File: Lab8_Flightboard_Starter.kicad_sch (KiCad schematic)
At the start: 66 parts, among them J1 Motor1, J10 ESC3_GND, J11 ESC4_VBAT, J12 ESC4_GND, J2 Motor2, J3 Motor3, J4 Motor4, J5 ESC1_VBAT, J6 ESC1_GND, J7 ESC2_VBAT, J8 ESC2_GND, J9 ESC3_VBAT, Q1 DMP6023LE-13, U1 Teensy4.0, U10 MPU6050_HiLetgo_GY521, U2 TPS62933, U4 LP5912-3.3DRV, U5 LP5912-3.3DRV, U6 NRF24L01_Breakout, U8 MPU6050_Adafruit, U9 LSM6DSO32_Adafruit

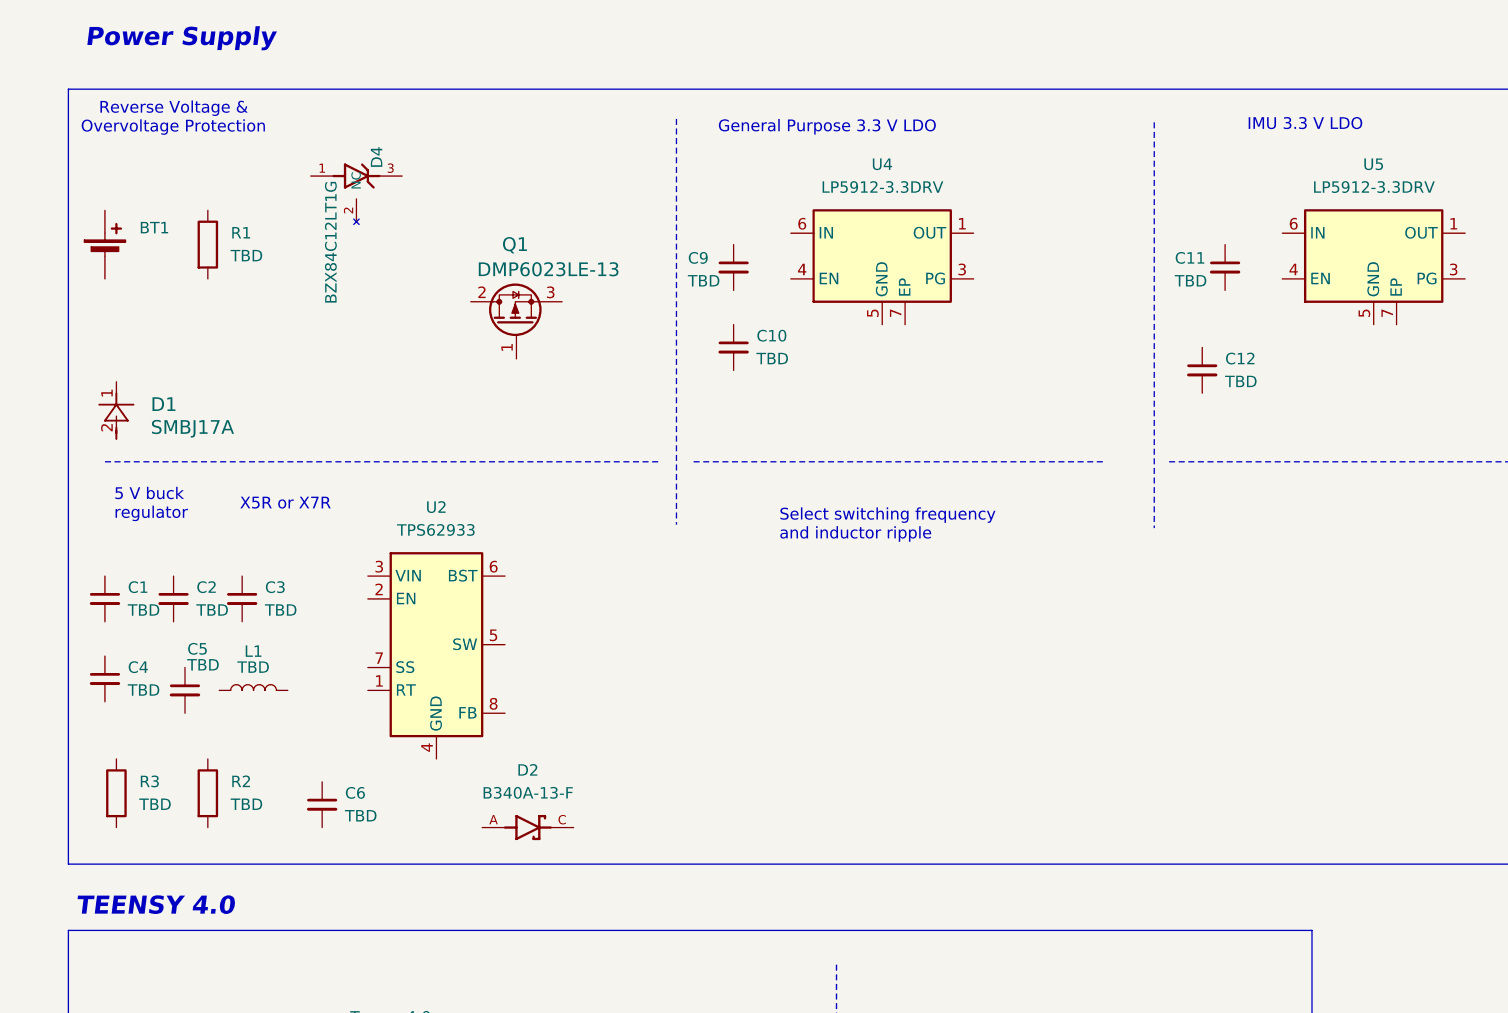
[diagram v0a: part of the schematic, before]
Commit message: Reverse voltage and 5V buck circuits
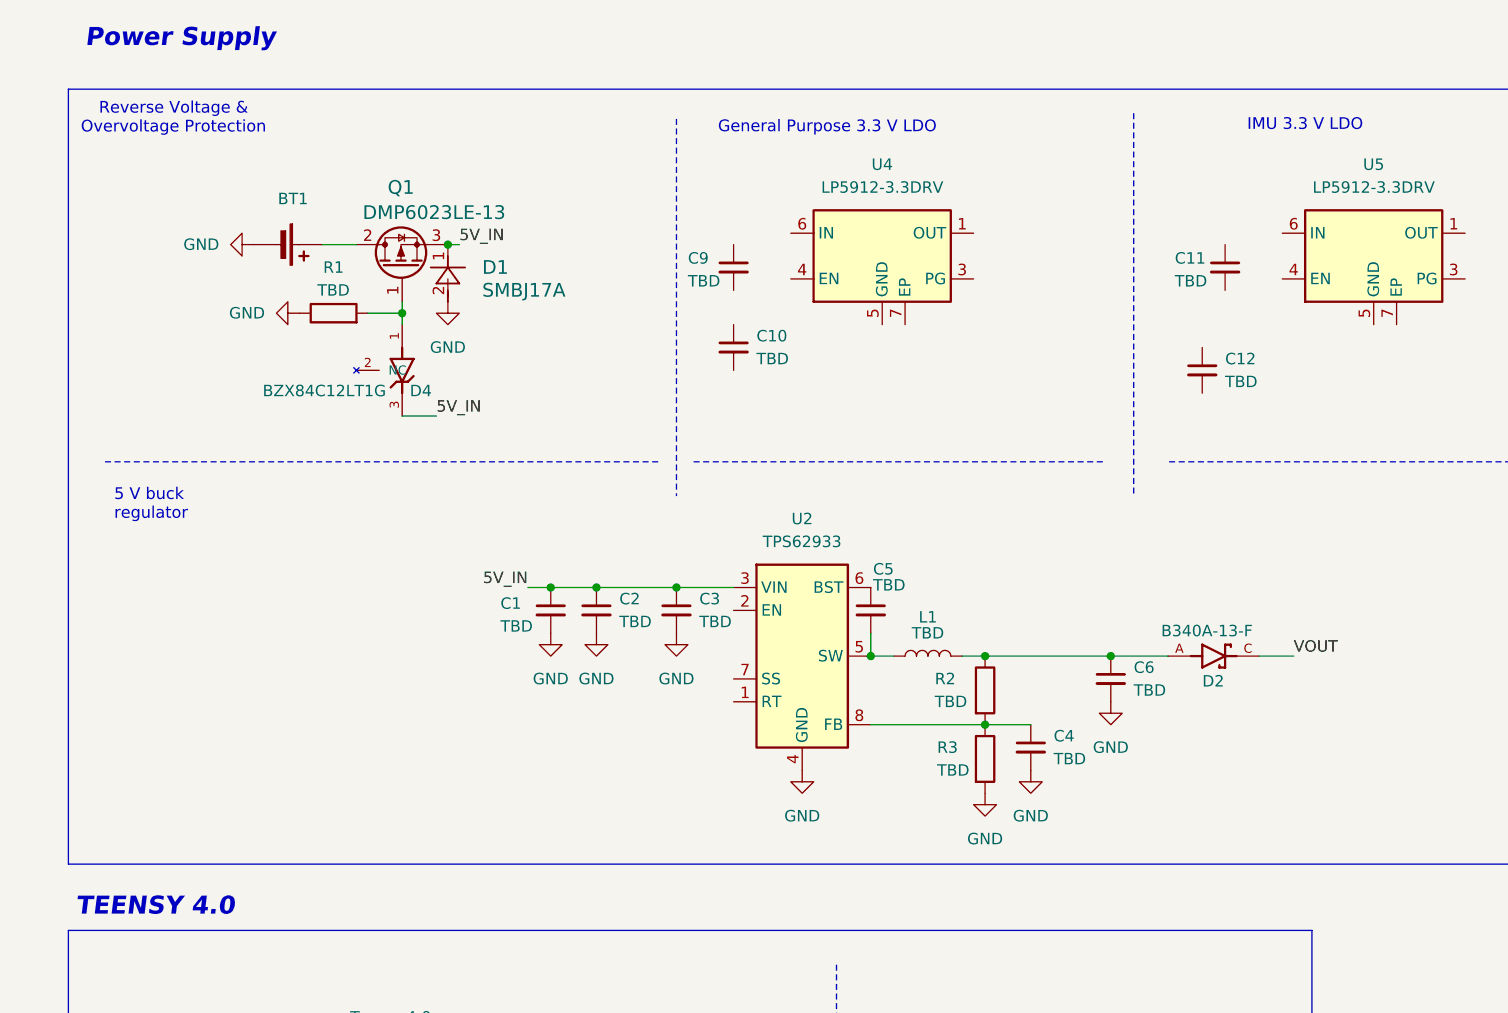
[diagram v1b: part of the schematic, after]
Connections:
- net at C4.1: now also R2.2, R3.1, U2.8 (FB)
- net GND: now reaches C4.2
- net GND: now also BT1.2 (-), C1.2, C2.2, C3.2, C6.2, D1.2, R1.1, R3.2, U2.4 (GND)
- net at C5.1: now also U2.6 (BST)
- net at C5.2: now also L1.1, U2.5 (SW)
- net at L1.2: now also C6.1, D2.A, R2.1
- net 5V_IN: now reaches C3.1
- net 5V_IN: now also C1.1, C2.1, D1.1, D4.3, Q1.3, U2.3 (VIN)
- net at R1.2: now also D4.1, Q1.1
- net at Q1.2: now also BT1.1 (+)
- net VOUT: now reaches D2.C
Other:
- note removed: "Select switching frequency and inductor ripple"
- note removed: "X5R or X7R"
- moved on the sheet: BT1, C1, C2, C3, C4, C5, C6, D1, D4, L1, Q1, R1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

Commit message: Circuit update V2
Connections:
- net GND: now also C4.1, U2.1 (RT), U5.5 (GND); no longer C4.2
- net at R2.2, R3.1, U2.8 (FB): no longer C4.1
- net at U2.7 (SS): now also C4.2
- net 5V_IN renamed LIPO_IN
- net VOUT renamed 5V_OUT
- no-connect marks 0 -> 1
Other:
- moved on the sheet: C1, C2, C3, C5, C6, D2, L1, R2, R3, U2

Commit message: Added values
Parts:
- C1, C2: value TBD -> 10u
- C3, C5: value TBD -> 0.1u
- C4: value TBD -> 33n
- C6: value TBD -> 20u
- L1: value TBD -> 6.8u
- R2: value TBD -> 55k
- R3: value TBD -> 10k
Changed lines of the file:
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@@
 		(in_pos_files yes)
 		(dnp no)
-		(fields_autoplaced yes)
 		(property "Reference" "C4"
-			(at 107.95 99.0538 0)
+			(at 104.394 96.774 0)
 			(show_name no)
 			(do_not_autoplace no)
@@
 					(size 1.27 1.27)
 				)
-				(justify left)
+				(justify right)
 			)
 		)
-		(property "Value" "TBD"
-			(at 107.95 96.5138 0)
+		(property "Value" "33n"
+			(at 104.394 99.06 0)
 			(show_name no)
 			(do_not_autoplace no)
@@
 					(size 1.27 1.27)
 				)
-				(justify left)
+				(justify right)
 			)
 		)
@@
 			)
 		)
-		(property "Value" "TBD"
+		(property "Value" "0.1u"
 			(at 129.794 81.026 0)
 			(show_name no)
@@
 			)
 		)
-		(property "Value" "TBD"
+		(property "Value" "10k"
 			(at 136.906 101.6 0)
 			(show_name no)
@@
 			)
 		)
-		(property "Value" "TBD"
+		(property "Value" "6.8u"
 			(at 135.89 86.36 90)
 			(show_name no)
@@
 			)
 		)
-		(property "Value" "TBD"
+		(property "Value" "55k"
 			(at 136.652 93.98 0)
 			(show_name no)
@@
 			)
 		)
-		(property "Value" "TBD"
+		(property "Value" "0.1u"
 			(at 106.68 85.0962 0)
 			(show_name no)
@@
 			)
 		)
-		(property "Value" "TBD"
+		(property "Value" "20u"
 			(at 149.86 92.7162 0)
 			(show_name no)
@@
 			)
 		)
-		(property "Value" "TBD"
+		(property "Value" "10u"
 			(at 84.582 85.598 0)
 			(show_name no)
@@
 			)
 		)
-		(property "Value" "TBD"
+		(property "Value" "10u"
 			(at 97.79 85.0962 0)
 			(show_name no)

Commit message: Motor signals
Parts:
- C6: value 20u -> 22u
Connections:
- net GND: now also J1.3 (Pin_3), J10.1 (Pin_1), J12.1 (Pin_1), J2.3 (Pin_3), J3.3 (Pin_3), J4.3 (Pin_3), J6.1 (Pin_1), J8.1 (Pin_1), R10.1, R12.1, R7.1, R8.1
- net MOTOR1: now reaches R6.1
- net MOTOR1: now also J1.1 (Pin_1), R7.2
- net M1_CMD: now reaches R6.2
- net MOTOR4: now reaches J4.1 (Pin_1)
- net MOTOR4: now also R12.2, R13.2
- net MOTOR3: now reaches R10.2
- net MOTOR3: now also J3.1 (Pin_1), R11.2
- net M4_CMD: now reaches R13.1
- net VBAT: now reaches J9.1 (Pin_1)
- net VBAT: now also BT1.1 (+), J11.1 (Pin_1), J5.1 (Pin_1), J7.1 (Pin_1), Q1.2
- net M2_CMD: now reaches R9.1
- net MOTOR2: now reaches R9.2
- net MOTOR2: now also J2.1 (Pin_1), R8.2
- net M3_CMD: now reaches R11.1
- no-connect marks 1 -> 5
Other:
- moved on the sheet: J1, J10, J11, J12, J2, J3, J4, J5, J6, J7, J8, J9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

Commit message: Edited circuits
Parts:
- C10, C11, C12, C9: value TBD -> 10u
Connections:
- net 5V_OUT: now also C9.1, U4.4 (EN), U4.6 (IN)
- net GND: now also C10.2, C11.2, C12.2, C13.2, C9.2, D3.1 (K), D6.1 (K), U4.5 (GND)
- net VBAT: now also R4.2
- net at R17.2: now also D3.2 (A)
- net 3.3V_GP: now reaches R15.1
- net 3.3V_GP: now also C10.1, U4.1 (OUT)
- net at R15.2: now also D6.2 (A)
- net at R5.2: now also C13.1, R4.1
- net 3.3V_IMU: now reaches C12.1
- net 3.3V_IMU: now also U5.1 (OUT)
- net at C11.1: now also U5.4 (EN), U5.6 (IN)
- net LIPO_IN renamed SYS_VIN
- no-connect marks 5 -> 9
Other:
- note removed: "Keep the ONE IMU module you bought; delete the other TWO symbols. U8: Adafruit MPU6050 | U10: HiLetgo GY-521 MPU6050 | U9: Adafruit LSM6DSO32 Use its matching footprint. All R/C/L values are TBD; complete wiring and pin allocation."
- moved on the sheet: C10, C11, C12, C13, C9, D3, D6, R15, R17, R4, U4

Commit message: More changes
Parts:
- removed U10: MPU6050_HiLetgo_GY521, IMU_Modules:MPU6050_HiLetgo_GY521, symbol IMU_Symbols:MPU6050_HiLetgo_GY521
- removed U8: MPU6050_Adafruit, IMU_Modules:MPU6050_Adafruit, symbol IMU_Symbols:MPU6050_Adafruit
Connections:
- net GND: now also R5.1, U6.1 (GND), U9.3 (GND)
- no-connect marks 9 -> 14
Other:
- note removed: "IMU OPTIONS - KEEP ONE, DELETE TWO"
- moved on the sheet: C13, C24, C25, R16, R4, R5, U9

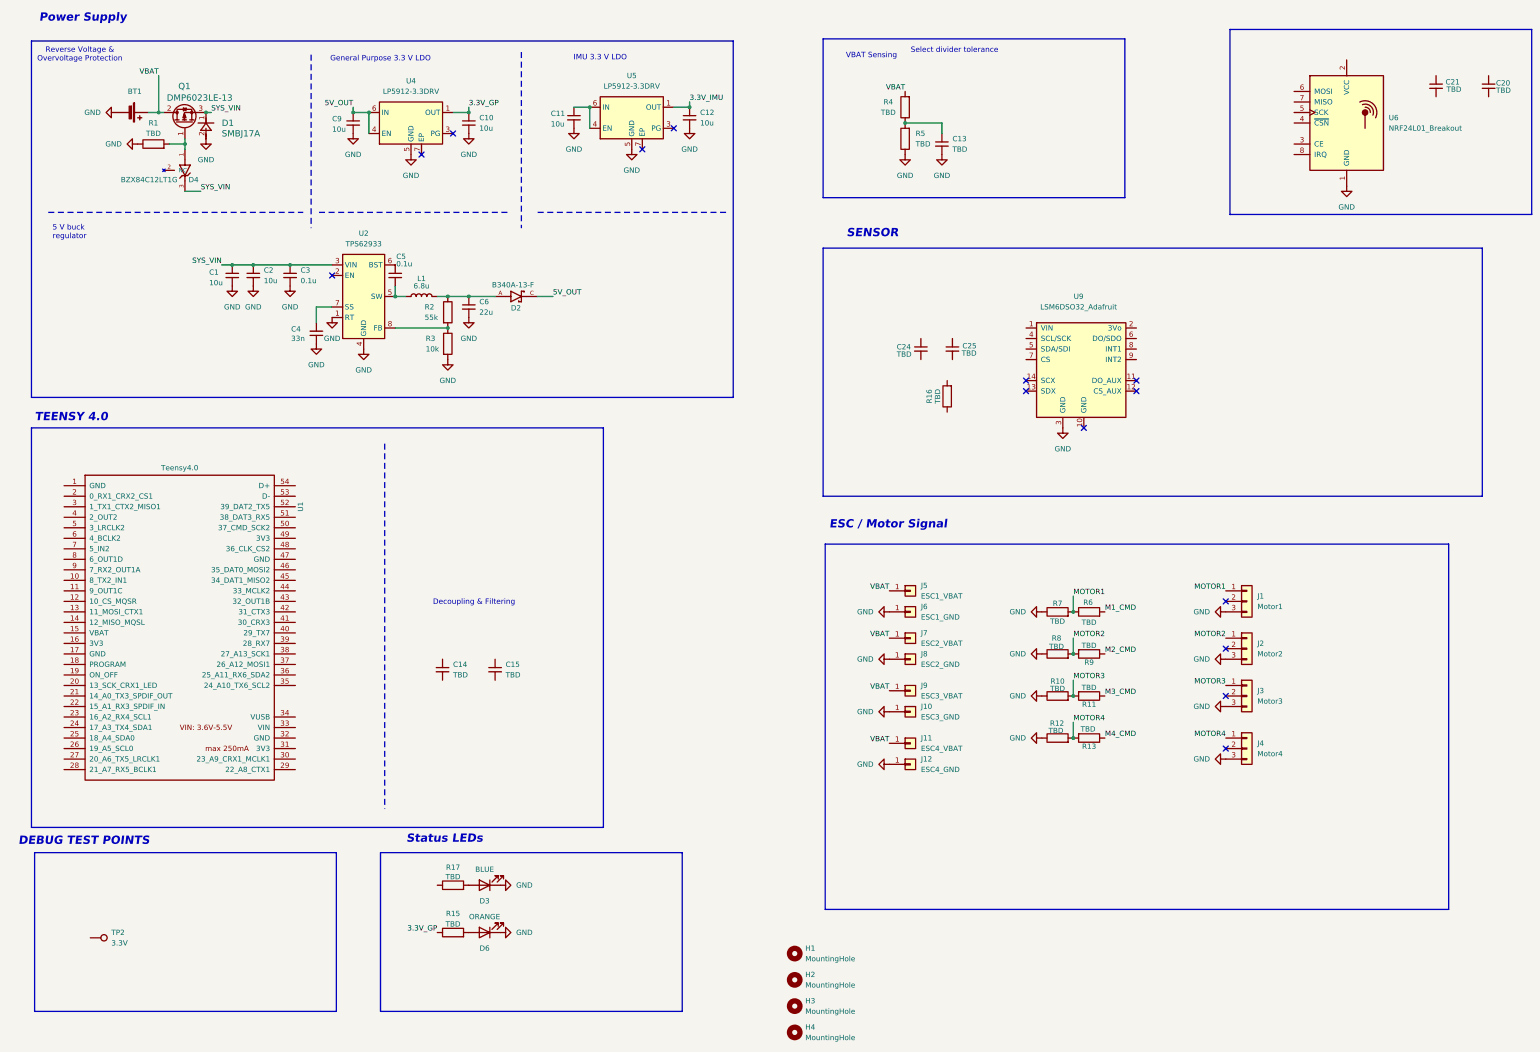
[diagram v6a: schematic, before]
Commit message: Added all component values
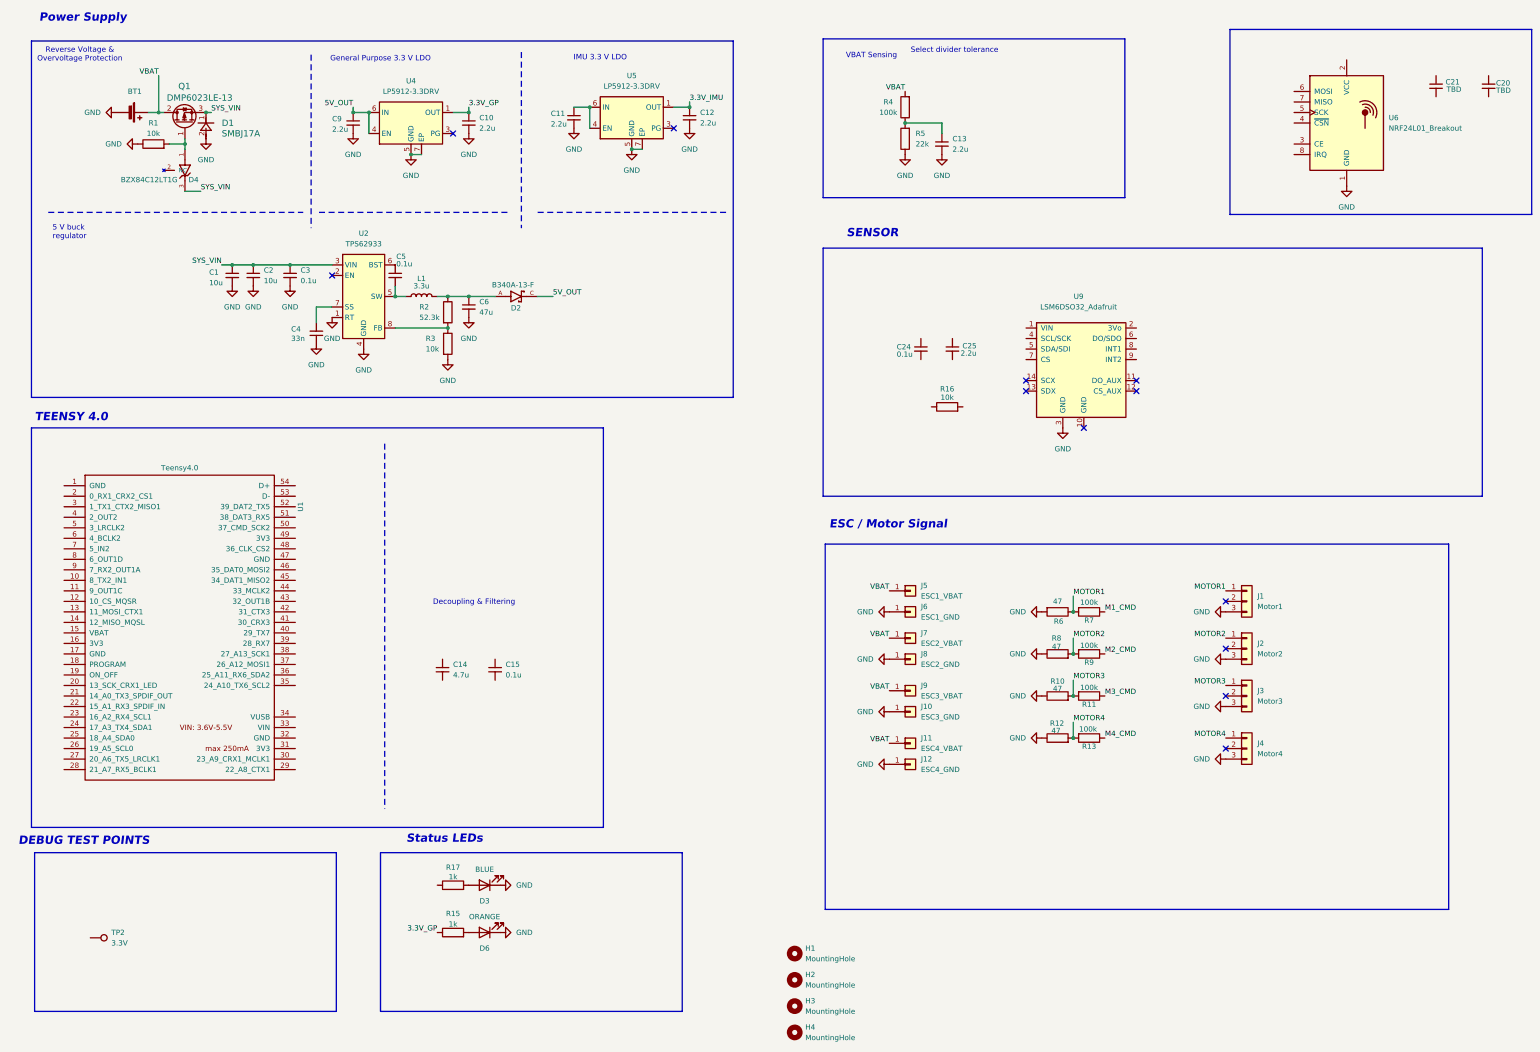
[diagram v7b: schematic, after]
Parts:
- C10, C11, C12, C9: value 10u -> 2.2u
- C13, C25: value TBD -> 2.2u
- C14: value TBD -> 4.7u
- C15, C24: value TBD -> 0.1u
- C6: value 22u -> 47u
- L1: value 6.8u -> 3.3u
- R1, R16: value TBD -> 10k
- R10, R12, R6, R8: value TBD -> 47
- R11, R13, R4, R7, R9: value TBD -> 100k
- R15, R17: value TBD -> 1k
- R2: value 55k -> 52.3k
- R5: value TBD -> 22k
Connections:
- net GND: now also R6.2, U4.7 (EP), U5.7 (EP); no longer R7.1
- net M1_CMD: now also R7.1; no longer R6.2
- no-connect marks 14 -> 12
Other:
- moved on the sheet: R16, R6, R7

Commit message: Forgot some values, updated it
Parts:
- C20: value TBD -> 0.1u
- C21: value TBD -> 2.2u
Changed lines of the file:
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@@
 			)
 		)
-		(property "Value" "TBD"
+		(property "Value" "0.1u"
 			(at 395.478 39.116 0)
 			(show_name no)
@@
 			)
 		)
-		(property "Value" "TBD"
+		(property "Value" "2.2u"
 			(at 383.54 38.862 0)
 			(show_name no)
